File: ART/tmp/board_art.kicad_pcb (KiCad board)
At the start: 2 copper layers, 94.7 x 67.7 mm, 4 parts

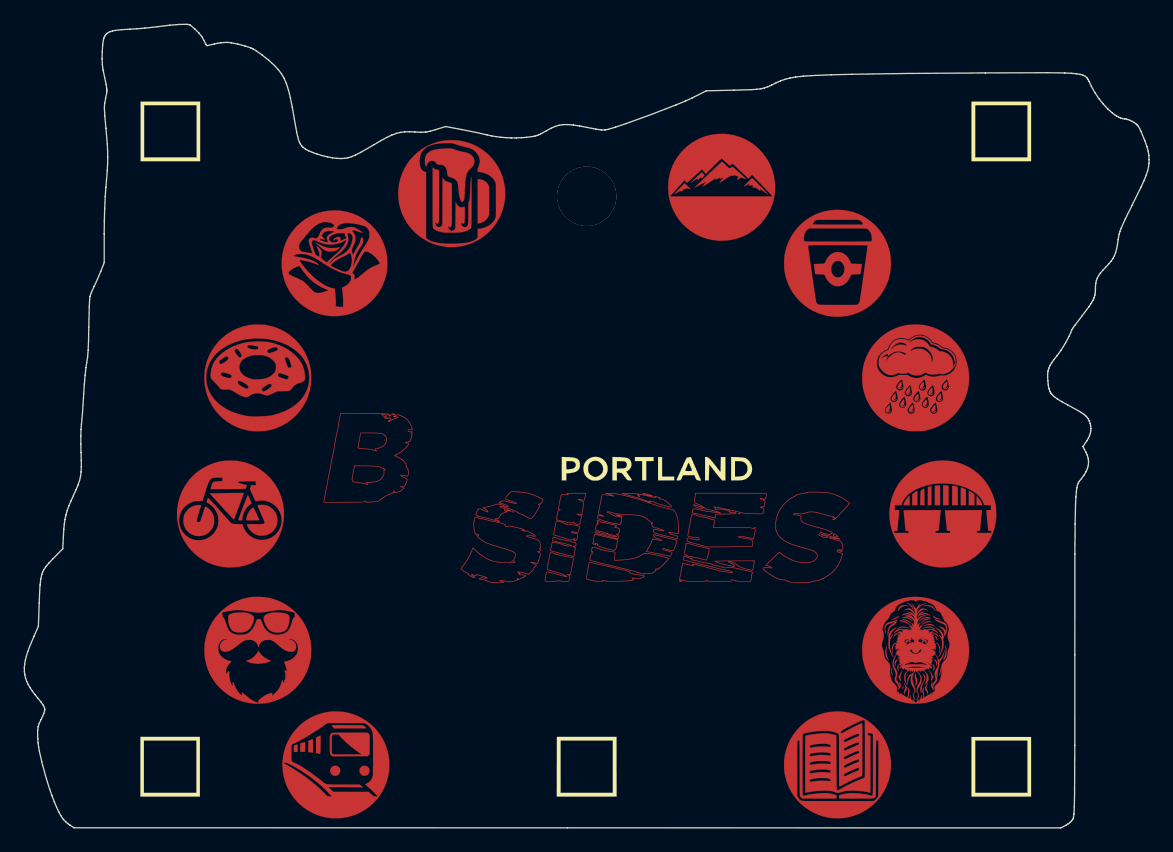
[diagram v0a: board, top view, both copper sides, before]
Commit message: removed bottom SAO, Added USB back, updated library paths
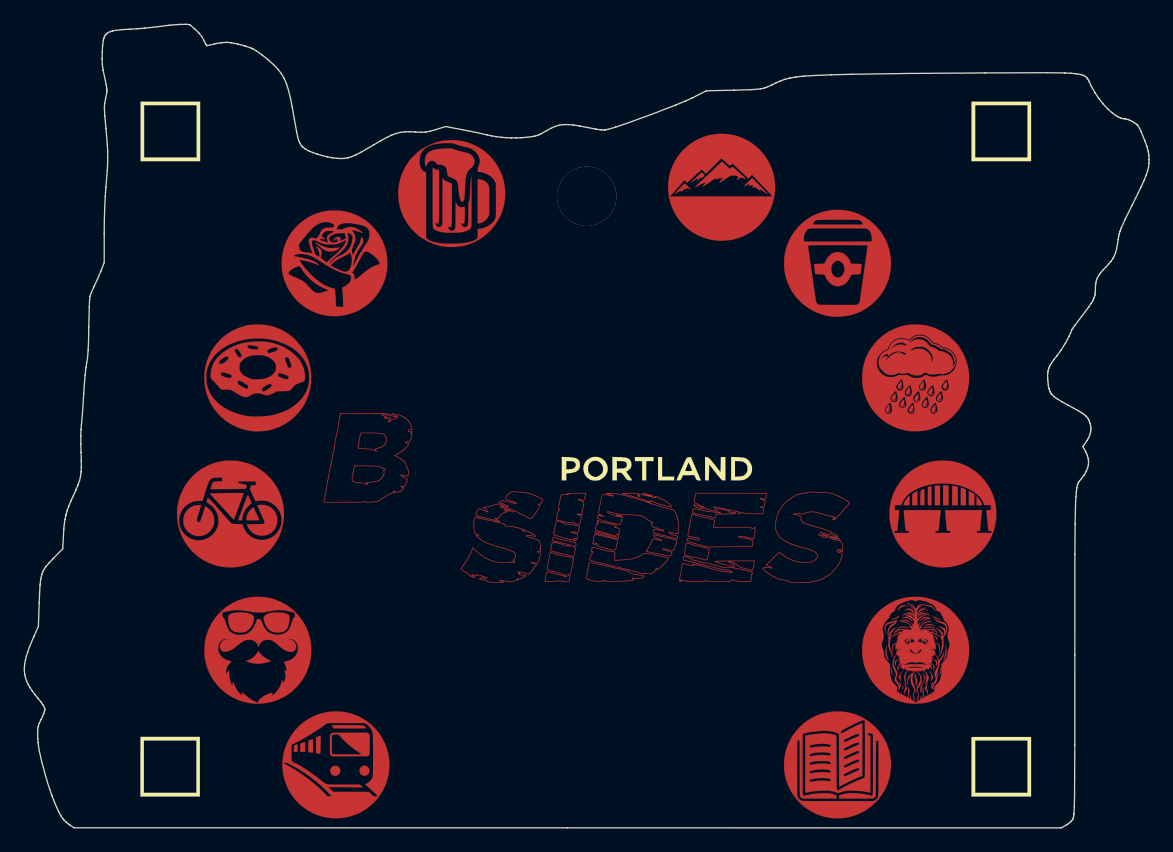
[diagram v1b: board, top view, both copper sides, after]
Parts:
- removed the G*** at (0.00, 0.00) (x3)
- added G*** (x3): LOGO, LOGO, F.Cu at (0.00, 0.00)
